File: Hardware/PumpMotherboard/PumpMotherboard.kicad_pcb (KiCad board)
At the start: 2 copper layers, 86.4 x 91.4 mm, 58 parts, among them J1 BTB, J2 AC_LEDs, J3 T_SENSOR, J4 T_SENSOR, J401 12V Input, J5 T_SENSOR, J6 SW_IN0, J7 SW_IN1, J8 SW_IN2, M1 Fan_4pin, M2 Fan_4pin, M3 Fan_4pin, M4 Fan_4pin, M5 Fan_4pin, M6 Fan_4pin, M7 Fan_4pin, M8 Fan_4pin, Q1 MMBT3904, Q2 MMBT3904, Q3 MMBT3904, Q4 MMBT3904, Q5 MMBT3904, Q6 MMBT3904, Q7 MMBT3904, Q8 MMBT3904, U2 AP63205WU

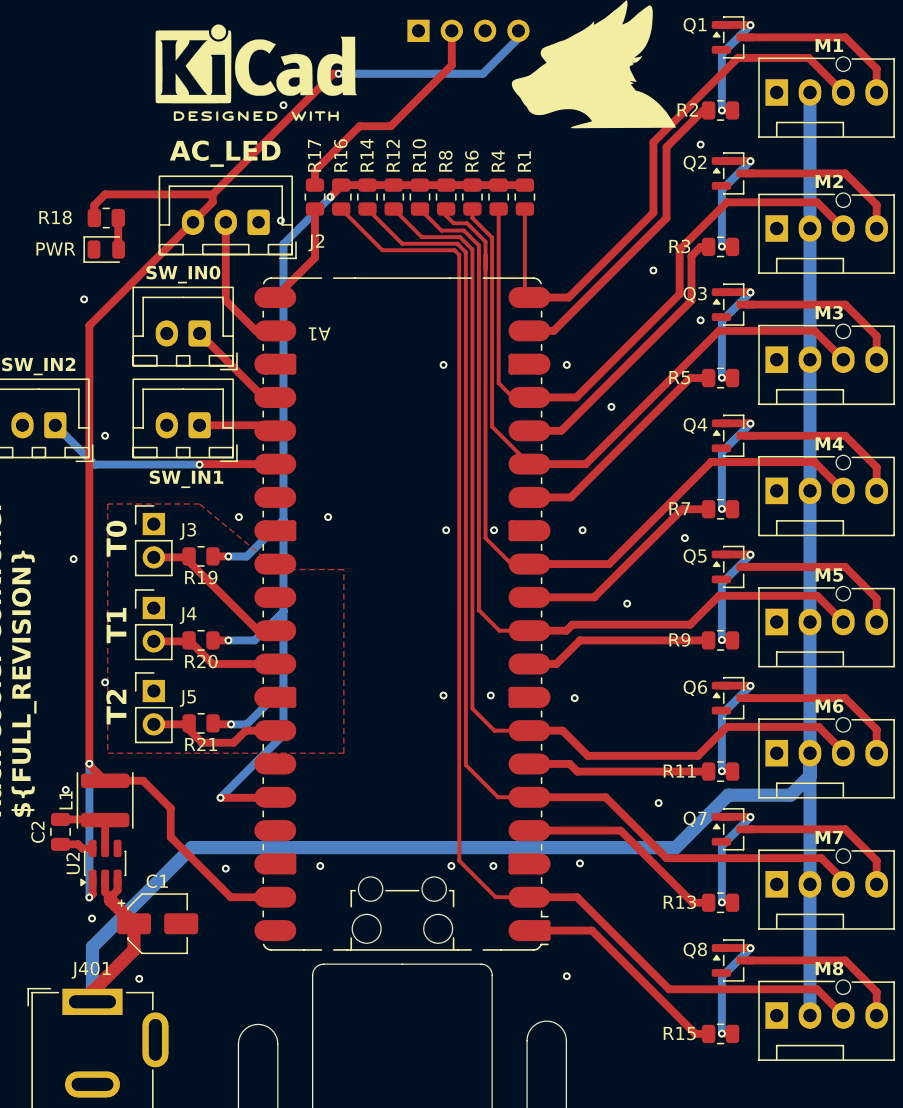
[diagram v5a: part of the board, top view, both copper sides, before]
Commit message: Thicken 12V trace
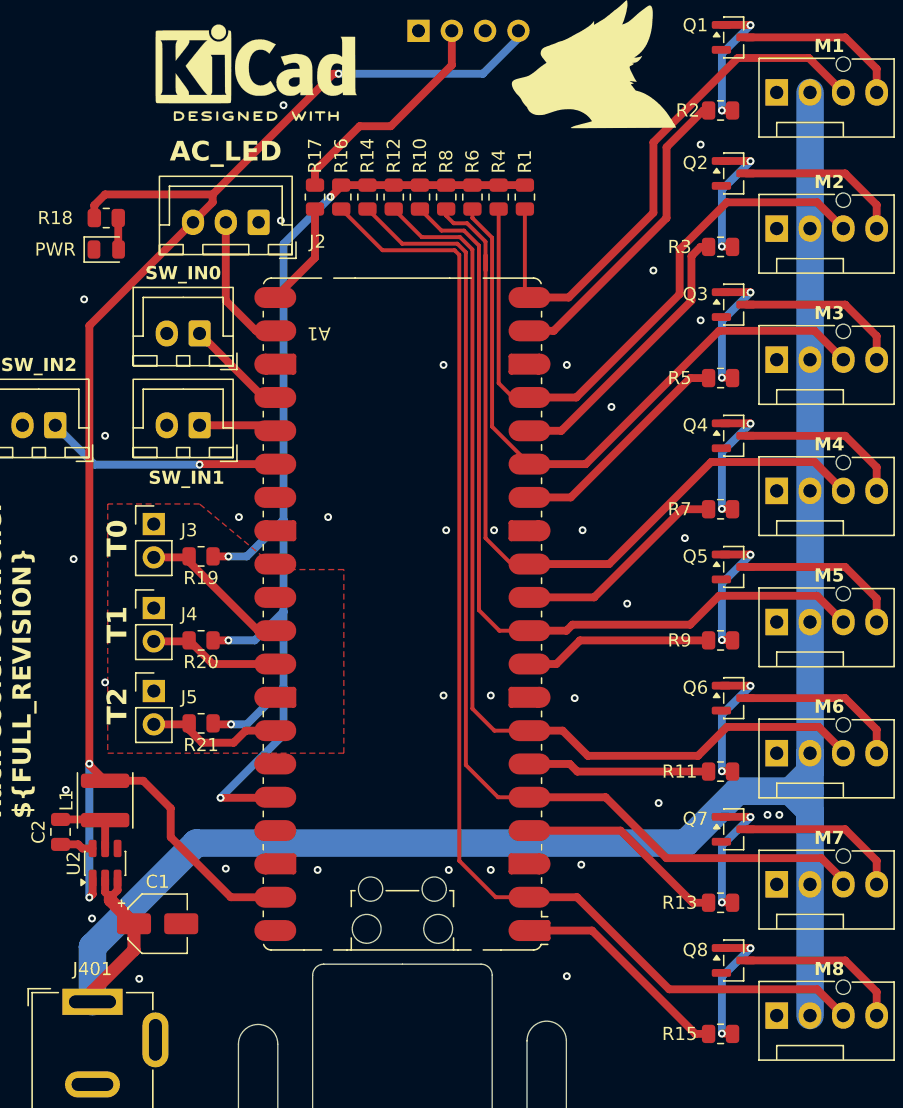
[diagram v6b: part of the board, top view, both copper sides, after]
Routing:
- net +12V: track 149.7 -> 152.6 mm
- net GND: vias 32 -> 34
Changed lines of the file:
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@@
+	)
+	(via
+		(at 164.2 108.7)
+		(size 0.6)
+		(drill 0.3)
+		(layers "F.Cu" "B.Cu")
+		(free yes)
+		(net "GND")
 	)
 	(via
@@
 	)
 	(via
-		(at 129.2 112.6)
+		(at 129 112.9)
 		(size 0.6)
 		(drill 0.3)
@@
 	)
 	(via
-		(at 139.2 112.6)
+		(at 139 112.9)
 		(size 0.6)
 		(drill 0.3)
@@
 	)
 	(via
-		(at 149 112.4)
+		(at 149.1 112.5)
 		(size 0.6)
 		(drill 0.3)
@@
 	)
 	(via
-		(at 142.4 112.6)
+		(at 142.2 112.9)
 		(size 0.6)
 		(drill 0.3)
@@
 	(via
 		(at 111.2 69.4)
+		(size 0.6)
+		(drill 0.3)
+		(layers "F.Cu" "B.Cu")
+		(free yes)
+		(net "GND")
+	)
+	(via
+		(at 163.3 108.7)
 		(size 0.6)
 		(drill 0.3)
@@
 	)
 	(segment
-		(start 119.4 111.2)
-		(end 156.3 111.2)
-		(width 1)
+		(start 166.54 106.9)
+		(end 166.54 53.6275)
+		(width 2.1)
 		(layer "B.Cu")
 		(net "+12V")
 	)
 	(segment
-		(start 156.3 111.2)
-		(end 160.3 107.2)
-		(width 1)
+		(start 166.54 124)
+		(end 166.54 106.9)
+		(width 2.1)
 		(layer "B.Cu")
 		(net "+12V")
 	)
 	(segment
-		(start 111.835 118.765)
-		(end 119.4 111.2)
-		(width 1)
+		(start 161 106.9)
+		(end 157.05 110.85)
+		(width 2.1)
 		(layer "B.Cu")
 		(net "+12V")
 	)
 	(segment
-		(start 166.54 53.6275)
-		(end 166.54 124)
-		(width 1)
+		(start 111.835 118.757032)
+		(end 111.835 122.9525)
+		(width 2.1)
 		(layer "B.Cu")
 		(net "+12V")
 	)
 	(segment
-		(start 166.54 105.715)
+		(start 166.54 109.3)
+		(end 166.54 108.4)
+		(width 2.1)
+		(layer "B.Cu")
+		(net "+12V")
+	)
+	(segment
+		(start 166.54 108.4)
+		(end 165.04 106.9)
+		(width 2.1)
+		(layer "B.Cu")
+		(net "+12V")
+	)
+	(segment
+		(start 165.04 106.9)
+		(end 161 106.9)
+		(width 2.1)
+		(layer "B.Cu")
+		(net "+12V")
+	)
+	(segment
+		(start 166.54 105.4)
 		(end 166.54 104)
-		(width 1)
+		(width 2.1)
 		(layer "B.Cu")
 		(net "+12V")
 	)
 	(segment
-		(start 160.3 107.2)
-		(end 165.055 107.2)
-		(width 1)
+		(start 165.04 106.9)
+		(end 166.54 105.4)
+		(width 2.1)
 		(layer "B.Cu")
 		(net "+12V")
 	)
 	(segment
-		(start 111.835 122.9525)
-		(end 111.835 118.765)
-		(width 1)
+		(start 119.742032 110.85)
+		(end 111.835 118.757032)
+		(width 2.1)
 		(layer "B.Cu")
 		(net "+12V")
 	)
 	(segment
-		(start 165.055 107.2)
-		(end 166.54 105.715)
-		(width 1)
+		(start 157.05 110.85)
+		(end 119.742032 110.85)
+		(width 2.1)
 		(layer "B.Cu")
 		(net "+12V")
@@
 	)
 	(segment
+		(start 120 79)
+		(end 125.353898 79)
+		(width 0.6)
+		(layer "F.Cu")
+		(net "/SW_1")
+	)
+	(segment
+		(start 125.353898 79)
+		(end 125.773898 79.42)
+		(width 0.6)
+		(layer "F.Cu")
+		(net "/SW_1")
+	)
+	(segment
 		(start 171.62 92.2)
 		(end 171.62 94)
@@
 	)
 	(segment
+		(start 120.04 81.96)
+		(end 120 82)
+		(width 0.6)
+		(layer "F.Cu")
+		(net "/SW_2")
+	)
+	(segment
+		(start 125.773898 81.96)
+		(end 120.04 81.96)
+		(width 0.6)
+		(layer "F.Cu")
+		(net "/SW_2")
+	)
+	(via
+		(at 120 82)
+		(size 0.6)
+		(drill 0.3)
+		(layers "F.Cu" "B.Cu")
+		(net "/SW_2")
+	)
+	(segment
+		(start 112 82)
+		(end 120 82)
+		(width 0.6)
+		(layer "B.Cu")
+		(net "/SW_2")
+	)
+	(segment
+		(start 109 79)
+		(end 112 82)
+		(width 0.6)
+		(layer "B.Cu")
+		(net "/SW_2")
+	)
+	(segment
+		(start 124.88 76.88)
+		(end 125.773898 76.88)
+		(width 0.6)
+		(layer "F.Cu")
+		(net "/SW_0")
+	)
+	(segment
+		(start 120 72)
+		(end 124.88 76.88)
+		(width 0.6)
+		(layer "F.Cu")
+		(net "/SW_0")
+	)
+	(segment
 		(start 161.6575 109.8)
 		(end 169.22 109.8)
@@
 		(net "Net-(M2-PWM)")
 	)
-	(segment
-		(start 120 79)
-		(end 125.353898 79)
-		(width 0.6)
-		(layer "F.Cu")
-		(net "/SW_1")
-	)
-	(segment
-		(start 125.353898 79)
-		(end 125.773898 79.42)
-		(width 0.6)
-		(layer "F.Cu")
-		(net "/SW_1")
-	)
-	(segment
-		(start 124.88 76.88)
-		(end 125.773898 76.88)
-		(width 0.6)
-		(layer "F.Cu")
-		(net "/SW_0")
-	)
-	(segment
-		(start 120 72)
-		(end 124.88 76.88)
-		(width 0.6)
-		(layer "F.Cu")
-		(net "/SW_0")
-	)
-	(segment
-		(start 120.04 81.96)
-		(end 120 82)
-		(width 0.6)
-		(layer "F.Cu")
-		(net "/SW_2")
-	)
-	(segment
-		(start 125.773898 81.96)
-		(end 120.04 81.96)
-		(width 0.6)
-		(layer "F.Cu")
-		(net "/SW_2")
-	)
-	(via
-		(at 120 82)
-		(size 0.6)
-		(drill 0.3)
-		(layers "F.Cu" "B.Cu")
-		(net "/SW_2")
-	)
-	(segment
-		(start 112 82)
-		(end 120 82)
-		(width 0.6)
-		(layer "B.Cu")
-		(net "/SW_2")
-	)
-	(segment
-		(start 109 79)
-		(end 112 82)
-		(width 0.6)
-		(layer "B.Cu")
-		(net "/SW_2")
-	)
 	(zone

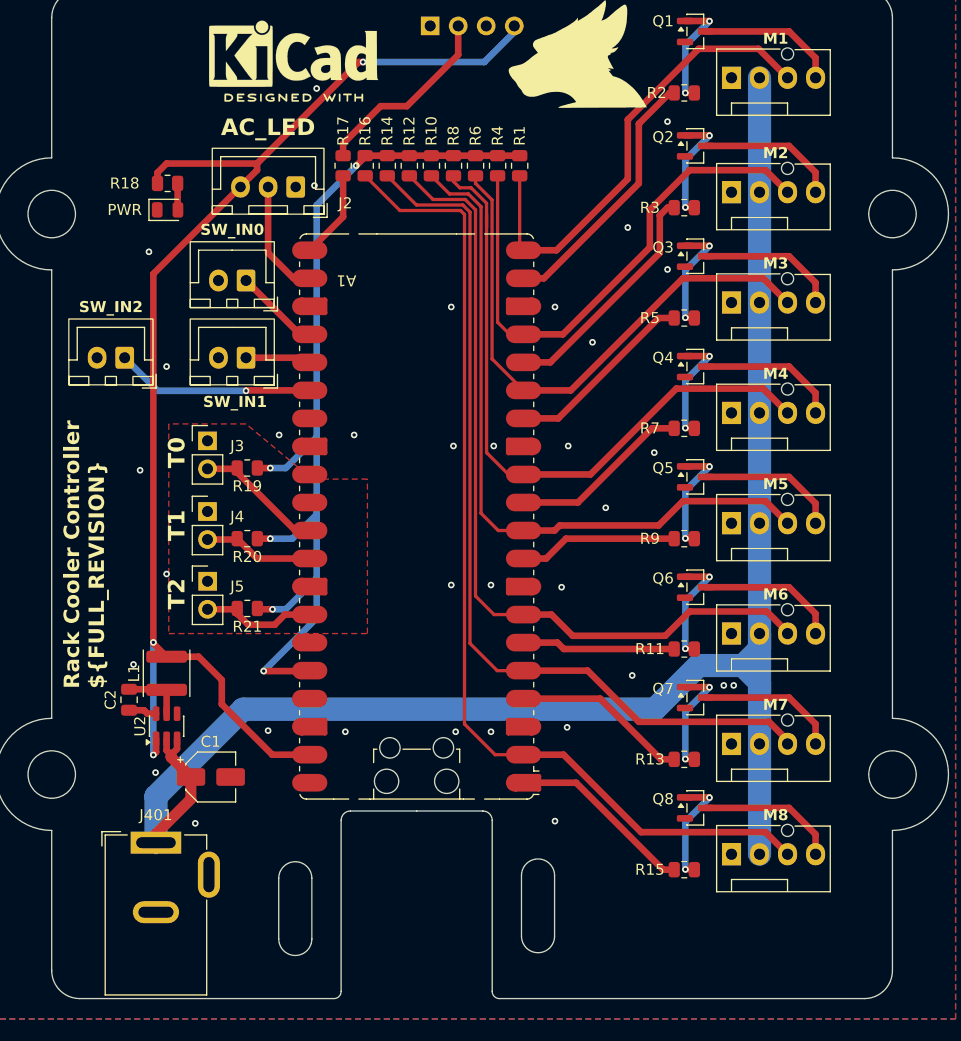
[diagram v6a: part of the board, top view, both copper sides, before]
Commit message: Add 12v power switching
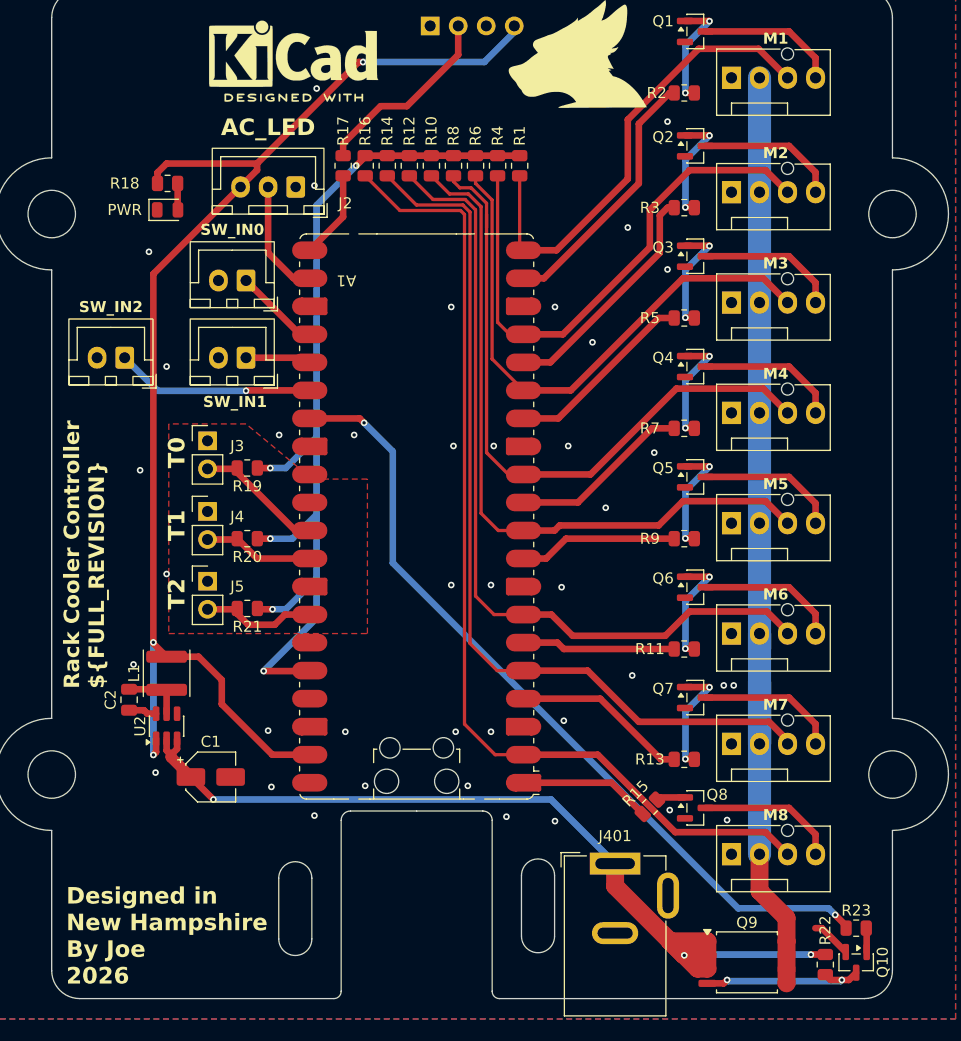
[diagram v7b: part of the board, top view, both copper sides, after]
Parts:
- added Q10: MMBT3904, Package_TO_SOT_SMD:SOT-23, F.Cu at (175.3, 133.8)
- added Q9: AO4407A, Package_SO:SOIC-8_5.3x5.3mm_P1.27mm, F.Cu at (165.4, 133.8)
- added R22: 10K, Resistor_SMD:R_0805_2012Metric, F.Cu at (172.5, 134.0)
- added R23: 1K, Resistor_SMD:R_0805_2012Metric, F.Cu at (175.3, 130.7)
- moved J401 41.7 mm to (153.4, 124.8)
- moved R15 6.50 mm to (156.6, 119.7), turned to 45 degrees
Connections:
- A1 pad 27: unconnected-(A1-GPIO21-Pad27) -> /LOAD_EN
- M1 pad 2: +12V -> 12V_SWITCHED
- M2 pad 2: +12V -> 12V_SWITCHED
- M3 pad 2: +12V -> 12V_SWITCHED
- M4 pad 2: +12V -> 12V_SWITCHED
- M5 pad 2: +12V -> 12V_SWITCHED
- M6 pad 2: +12V -> 12V_SWITCHED
- M7 pad 2: +12V -> 12V_SWITCHED
- M8 pad 2: +12V -> 12V_SWITCHED
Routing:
- net 12V_SWITCHED: track 0.00 -> 90.1 mm
- net /LOAD_EN: track 0.00 -> 73.8 mm, vias 0 -> 2
- net +12V: track 152.6 -> 85.8 mm, vias 0 -> 3
- net Net-(Q10-C): track 0.00 -> 15.7 mm, vias 0 -> 2
- net Net-(Q8-B): track 10.4 -> 2.62 mm, vias 2 -> 0
- net /PWM_7: track 16.9 -> 12.0 mm
- net GND: track 0.00 -> 3.65 mm, vias 34 -> 40
- net Net-(Q10-B): track 0.00 -> 2.18 mm

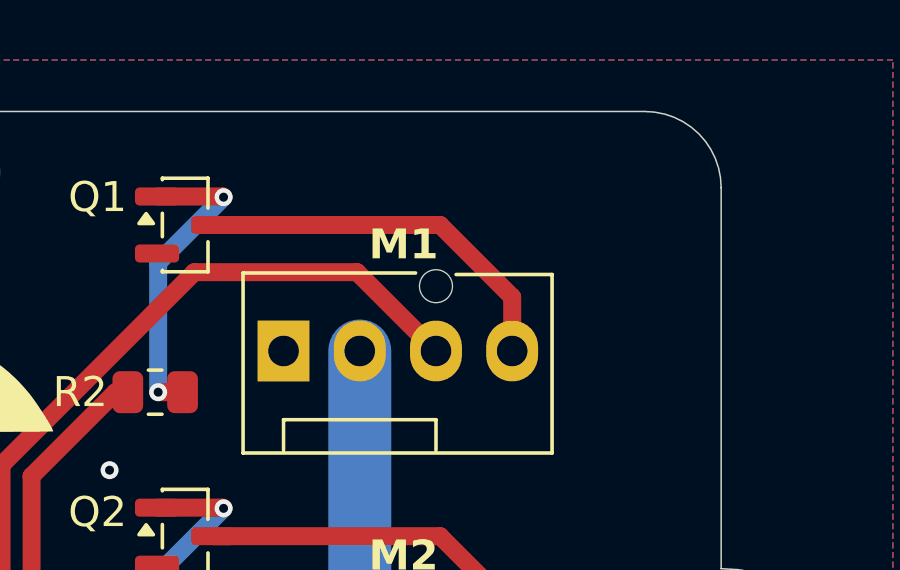
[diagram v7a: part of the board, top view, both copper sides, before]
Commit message: Add flyback protection
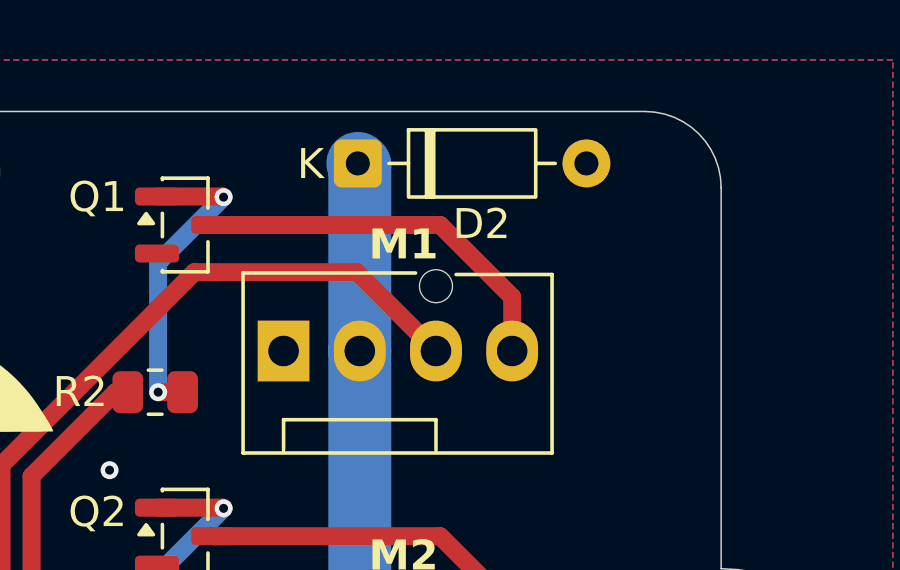
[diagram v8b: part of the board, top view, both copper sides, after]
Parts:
- added D2: 1N4148, Diode_THT:D_DO-35_SOD27_P7.62mm_Horizontal, F.Cu at (166.5, 47.4)
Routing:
- net 12V_SWITCHED: track 90.1 -> 96.4 mm
